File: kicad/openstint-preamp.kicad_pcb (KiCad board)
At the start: 2 copper layers, 50.5 x 50.5 mm, 43 parts, among them J1 Phoenix PTS 1,5/ 2-5,0-H, J2 OUT, J3 Vin, J4 VNA_IN, J5 CAL_O, J6 CAL_S, J7 CAL_L, Q1 BFR106

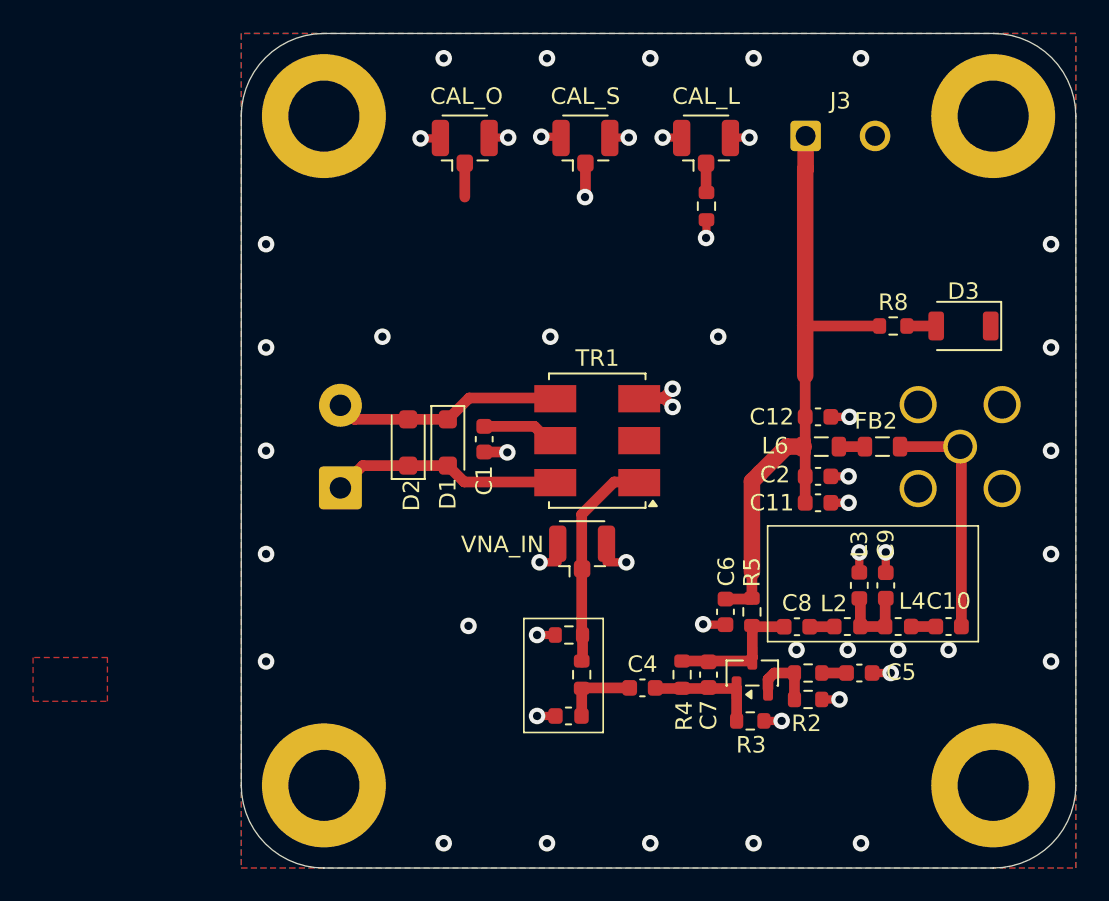
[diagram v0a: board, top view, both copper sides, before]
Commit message: matching network, battery connection, oshw logo
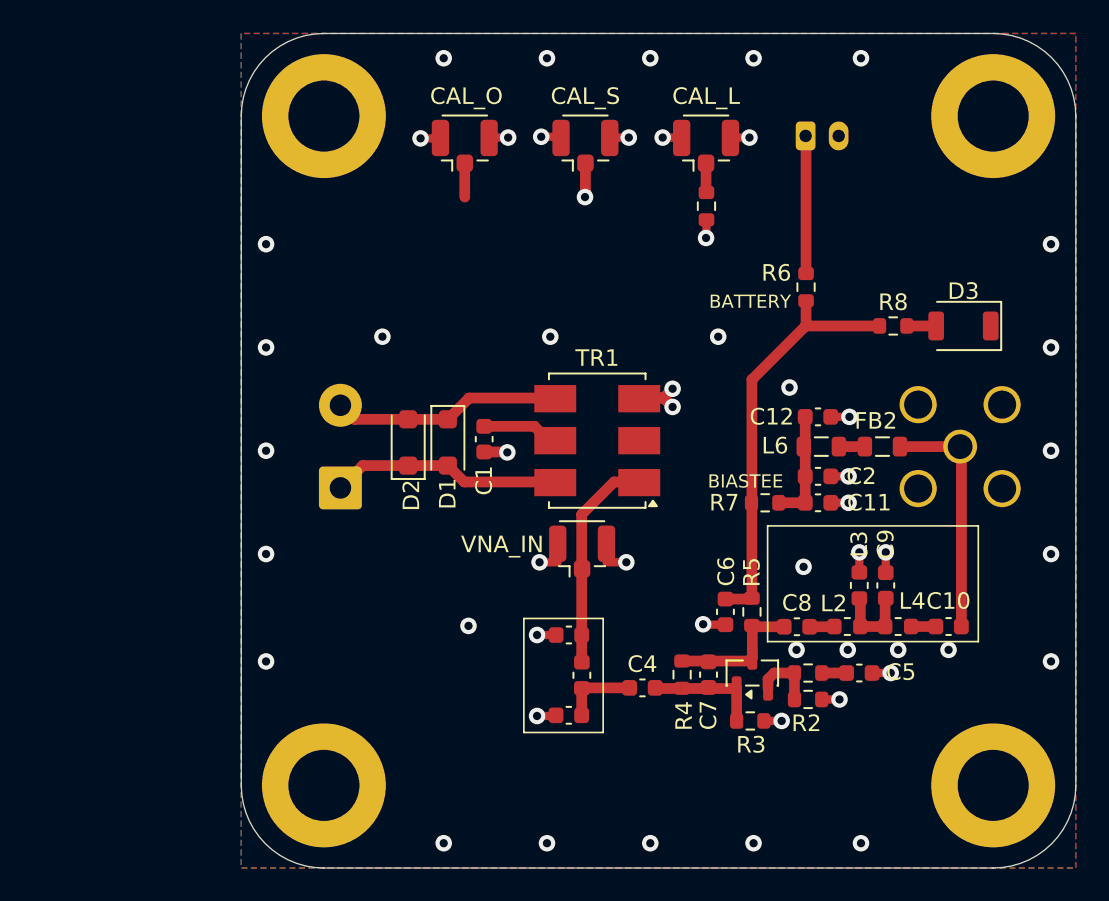
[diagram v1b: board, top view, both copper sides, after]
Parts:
- removed L5: ?, Inductor_SMD:L_0603_1608Metric
- removed R12: 0, Resistor_SMD:R_0603_1608Metric
- added C13: 1500p, Capacitor_SMD:C_0603_1608Metric, F.Cu at (134.8, 106.3)
- added C3: dnp, Capacitor_SMD:C_0603_1608Metric, F.Cu at (134.8, 101.4)
- added R6: 0, Resistor_SMD:R_0603_1608Metric, F.Cu at (149.2, 80.3)
- added R7: 0, Resistor_SMD:R_0603_1608Metric, F.Cu at (146.7, 93.4)
- added SYM1: Logo_Open_Hardware_Small, Symbol:OSHW-Logo2_9.8x8mm_SilkScreen, B.Cu at (130.8, 70.8)
- J3: footprint Connector_Wire:SolderWire-0.25sqmm_1x02_P4.2mm_D0.65mm_OD1.7mm -> Connector_JST:JST_PH_B2B-PH-K_1x02_P2.00mm_Vertical; moved to B.Cu
- L1: value 0 -> 820n; footprint Resistor_SMD:R_0603_1608Metric -> Inductor_SMD:L_0603_1608Metric
- moved L1 2.56 mm to (135.6, 103.8), turned to -90 degrees
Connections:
- C11 pad 2: VCC -> VBIAS
- C12 pad 2: VCC -> VBIAS
- C2 pad 2: VCC -> VBIAS
- C4 pad 1: Net-(C4-Pad1) -> Net-(C13-Pad1)
- J3 pad 1: VCC -> +BATT
- L1 pad 1: GND -> /loop_unbal
- L1 pad 2: /loop_unbal -> Net-(C13-Pad1)
- L6 pad 2: VCC -> VBIAS
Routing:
- net VCC: track 39.4 -> 25.5 mm
- net +BATT: track 0.00 -> 8.34 mm
- net VBIAS: track 0.00 -> 6.80 mm
- net Net-(C4-Pad1): track 4.61 -> 0.00 mm
- net Net-(C13-Pad1): track 0.00 -> 4.61 mm
- net GND: vias 52 -> 54
- removed copper zone on F.Cu, net VCC
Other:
- board text added: "BATTERY"
- board text added: "BIASTEE"
